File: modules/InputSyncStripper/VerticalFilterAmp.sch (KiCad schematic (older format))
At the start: 12 parts

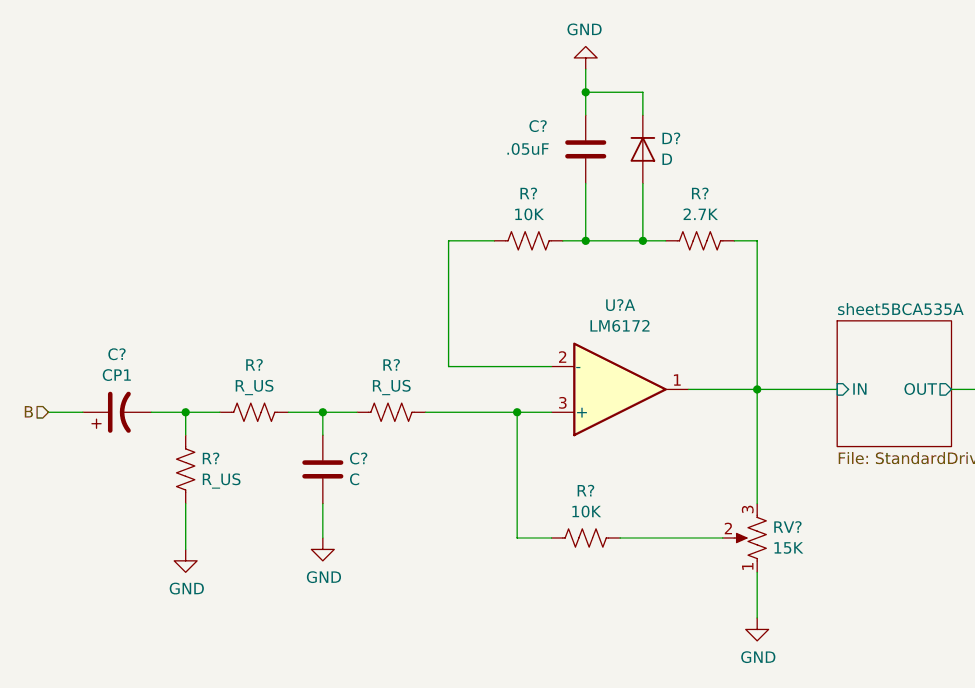
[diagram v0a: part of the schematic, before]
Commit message: fix some ERC issues; assign symbols
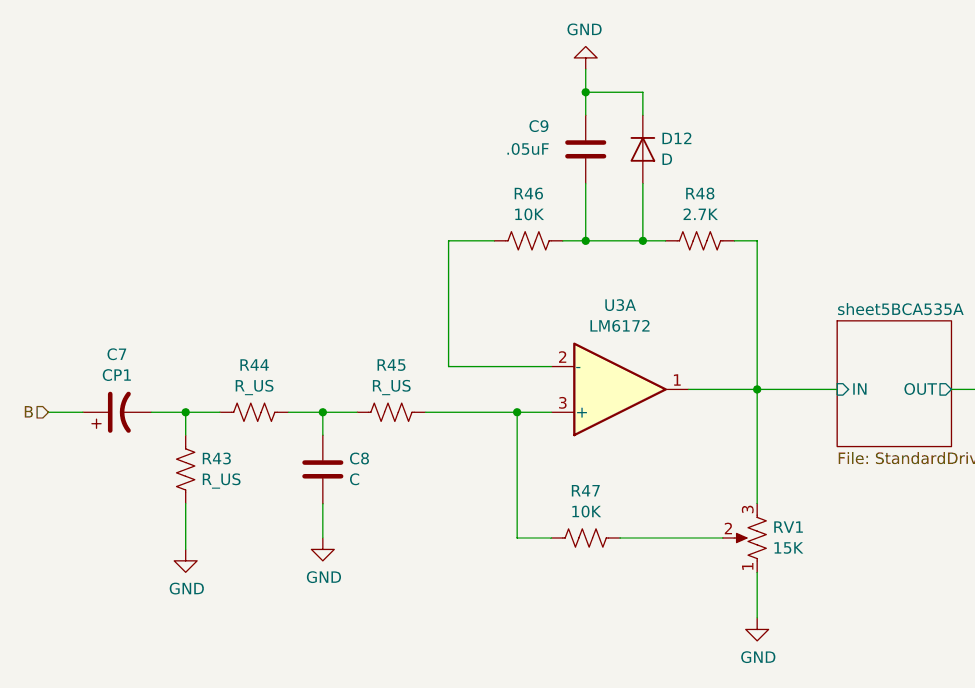
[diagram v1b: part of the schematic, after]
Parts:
- gave numbers to parts that had none: 12
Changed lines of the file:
@@
 EESchema Schematic File Version 4
-LIBS:SIP-cache
+LIBS:InputSyncStripper-cache
 EELAYER 26 0
 EELAYER END
@@
 $EndDescr
 $Comp
-L Amplifier_Operational:LM6172 U?
+L Amplifier_Operational:LM6172 U3
 U 1 1 5BCA52BB
 P 4700 3700
-F 0 "U?" H 4700 3333 50  0000 C CNN
+F 0 "U3" H 4700 3333 50  0000 C CNN
 F 1 "LM6172" H 4700 3424 50  0000 C CNN
 F 2 "" H 4700 3700 50  0001 C CNN
@@
 $EndSheet
 $Comp
-L Device:R_US R?
+L Device:R_US R48
 U 1 1 5BCA537D
 P 5050 3050
-F 0 "R?" V 4845 3050 50  0000 C CNN
+F 0 "R48" V 4845 3050 50  0000 C CNN
 F 1 "2.7K" V 4936 3050 50  0000 C CNN
 F 2 "" V 5090 3040 50  0001 C CNN
@@
 $EndComp
 $Comp
-L Device:R_US R?
+L Device:R_US R46
 U 1 1 5BCA543E
 P 4300 3050
-F 0 "R?" V 4095 3050 50  0000 C CNN
+F 0 "R46" V 4095 3050 50  0000 C CNN
 F 1 "10K" V 4186 3050 50  0000 C CNN
 F 2 "" V 4340 3040 50  0001 C CNN
@@
 Connection ~ 5300 3700
 $Comp
-L Device:R_POT_US RV?
+L Device:R_POT_US RV1
 U 1 1 5BCA5542
 P 5300 4350
-F 0 "RV?" H 5232 4304 50  0000 R CNN
+F 0 "RV1" H 5232 4304 50  0000 R CNN
 F 1 "15K" H 5232 4395 50  0000 R CNN
 F 2 "" H 5300 4350 50  0001 C CNN
@@
 $EndComp
 $Comp
-L power:GND #PWR?
+L power:GND #PWR023
 U 1 1 5BCA55A7
 P 5300 4700
-F 0 "#PWR?" H 5300 4450 50  0001 C CNN
+F 0 "#PWR023" H 5300 4450 50  0001 C CNN
 F 1 "GND" H 5305 4527 50  0000 C CNN
 F 2 "" H 5300 4700 50  0001 C CNN
@@
 	5300 4200 5300 3700
 $Comp
-L Device:R_US R?
+L Device:R_US R47
 U 1 1 5BCA5671
 P 4550 4350
-F 0 "R?" V 4345 4350 50  0000 C CNN
+F 0 "R47" V 4345 4350 50  0000 C CNN
 F 1 "10K" V 4436 4350 50  0000 C CNN
 F 2 "" V 4590 4340 50  0001 C CNN
@@
 	4250 3800 4400 3800
 $Comp
-L Device:C C?
+L Device:C C9
 U 1 1 5BCA585A
 P 4550 2650
-F 0 "C?" H 4300 2750 50  0000 L CNN
+F 0 "C9" H 4300 2750 50  0000 L CNN
 F 1 ".05uF" H 4200 2650 50  0000 L CNN
 F 2 "" H 4588 2500 50  0001 C CNN
@@
 $EndComp
 $Comp
-L Device:D D?
+L Device:D D12
 U 1 1 5BCA5A8B
 P 4800 2650
-F 0 "D?" V 4754 2729 50  0000 L CNN
+F 0 "D12" V 4754 2729 50  0000 L CNN
 F 1 "D" V 4845 2729 50  0000 L CNN
 F 2 "" H 4800 2650 50  0001 C CNN
@@
 $EndComp
 $Comp
-L power:GND #PWR?
+L power:GND #PWR022
 U 1 1 5BCA5BA5
 P 4550 2300
-F 0 "#PWR?" H 4550 2050 50  0001 C CNN
+F 0 "#PWR022" H 4550 2050 50  0001 C CNN
 F 1 "GND" H 4555 2127 50  0000 C CNN
 F 2 "" H 4550 2300 50  0001 C CNN
@@
 	4800 3050 4900 3050
 $Comp
-L Device:R_US R?
+L Device:R_US R45
 U 1 1 5BCA6118
 P 3700 3800
-F 0 "R?" V 3495 3800 50  0000 C CNN
+F 0 "R45" V 3495 3800 50  0000 C CNN
 F 1 "R_US" V 3586 3800 50  0000 C CNN
 F 2 "" V 3740 3790 50  0001 C CNN
@@
 $EndComp
 $Comp
-L Device:R_US R?
+L Device:R_US R44
 U 1 1 5BCA6199
 P 3100 3800
-F 0 "R?" V 2895 3800 50  0000 C CNN
+F 0 "R44" V 2895 3800 50  0000 C CNN
 F 1 "R_US" V 2986 3800 50  0000 C CNN
 F 2 "" V 3140 3790 50  0001 C CNN
@@
 $EndComp
 $Comp
-L Device:R_US R?
+L Device:R_US R43
 U 1 1 5BCA61F8
 P 2800 4050
-F 0 "R?" H 2868 4096 50  0000 L CNN
+F 0 "R43" H 2868 4096 50  0000 L CNN
 F 1 "R_US" H 2868 4005 50  0000 L CNN
 F 2 "" V 2840 4040 50  0001 C CNN
@@
 $EndComp
 $Comp
-L Device:CP1 C?
+L Device:CP1 C7
 U 1 1 5BCA625D
 P 2500 3800
-F 0 "C?" V 2752 3800 50  0000 C CNN
+F 0 "C7" V 2752 3800 50  0000 C CNN
 F 1 "CP1" V 2661 3800 50  0000 C CNN
 F 2 "" H 2500 3800 50  0001 C CNN
@@
 $EndComp
 $Comp
-L Device:C C?
+L Device:C C8
 U 1 1 5BCA6305
 P 3400 4050
-F 0 "C?" H 3515 4096 50  0000 L CNN
+F 0 "C8" H 3515 4096 50  0000 L CNN
 F 1 "C" H 3515 4005 50  0000 L CNN
 F 2 "" H 3438 3900 50  0001 C CNN
@@
 $EndComp
 $Comp
-L power:GND #PWR?
+L power:GND #PWR020
 U 1 1 5BCA63C4
 P 2800 4400
-F 0 "#PWR?" H 2800 4150 50  0001 C CNN
+F 0 "#PWR020" H 2800 4150 50  0001 C CNN
 F 1 "GND" H 2805 4227 50  0000 C CNN
 F 2 "" H 2800 4400 50  0001 C CNN
@@
 $EndComp
 $Comp
-L power:GND #PWR?
+L power:GND #PWR021
 U 1 1 5BCA640A
 P 3400 4350
-F 0 "#PWR?" H 3400 4100 50  0001 C CNN
+F 0 "#PWR021" H 3400 4100 50  0001 C CNN
 F 1 "GND" H 3405 4177 50  0000 C CNN
 F 2 "" H 3400 4350 50  0001 C CNN

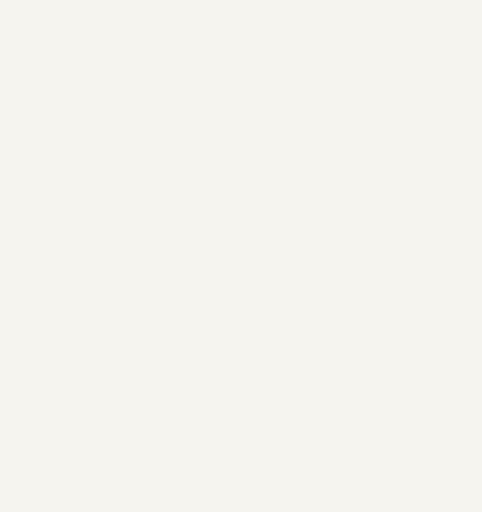
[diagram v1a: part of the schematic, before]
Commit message: added power pins for opamps and tied inputs of unused amp
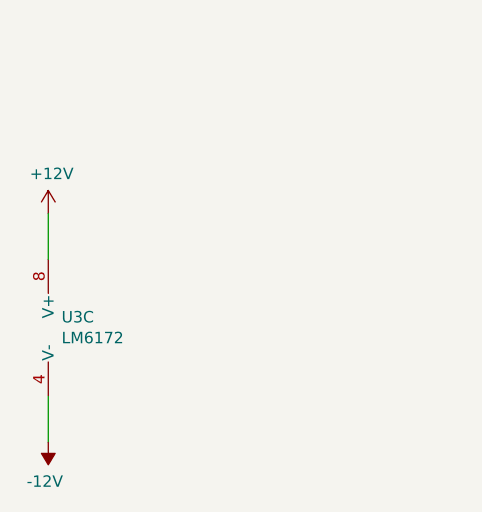
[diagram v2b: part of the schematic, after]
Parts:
- added unit 3 of U3
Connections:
- new net +12V: U3.8 (V+)
- new net -12V: U3.4 (V-)
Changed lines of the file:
@@
 Wire Wire Line
 	6150 3700 6500 3700
+$Comp
+L Amplifier_Operational:LM6172 U?
+U 3 1 5BCFED9F
+P 1150 7000
+AR Path="/5BC7EA60/5BCFED9F" Ref="U?"  Part="3"
+AR Path="/5BCA510D/5BCFED9F" Ref="U3"  Part="3"
+F 0 "U3" H 1108 7046 50  0000 L CNN
+F 1 "LM6172" H 1108 6955 50  0000 L CNN
+F 2 "" H 1150 7000 50  0001 C CNN
+F 3 "http://www.ti.com/lit/ds/symlink/lm6172.pdf" H 1150 7000 50  0001 C CNN
+	3    1150 7000
+	1    0    0    -1
+$EndComp
+$Comp
+L power:+12V #PWR?
+U 1 1 5BCFEDA6
+P 1050 6500
+AR Path="/5BC7EA60/5BCFEDA6" Ref="#PWR?"  Part="1"
+AR Path="/5BCA510D/5BCFEDA6" Ref="#PWR0114"  Part="1"
+F 0 "#PWR0114" H 1050 6350 50  0001 C CNN
+F 1 "+12V" H 1065 6673 50  0000 C CNN
+F 2 "" H 1050 6500 50  0001 C CNN
+F 3 "" H 1050 6500 50  0001 C CNN
+	1    1050 6500
+	1    0    0    -1
+$EndComp
+$Comp
+L power:-12V #PWR?
+U 1 1 5BCFEDAC
+P 1050 7500
+AR Path="/5BC7EA60/5BCFEDAC" Ref="#PWR?"  Part="1"
+AR Path="/5BCA510D/5BCFEDAC" Ref="#PWR0115"  Part="1"
+F 0 "#PWR0115" H 1050 7600 50  0001 C CNN
+F 1 "-12V" H 1065 7673 50  0000 C CNN
+F 2 "" H 1050 7500 50  0001 C CNN
+F 3 "" H 1050 7500 50  0001 C CNN
+	1    1050 7500
+	-1   0    0    1
+$EndComp
+Wire Wire Line
+	1050 7500 1050 7300
+Wire Wire Line
+	1050 6700 1050 6500
 $EndSCHEMATC

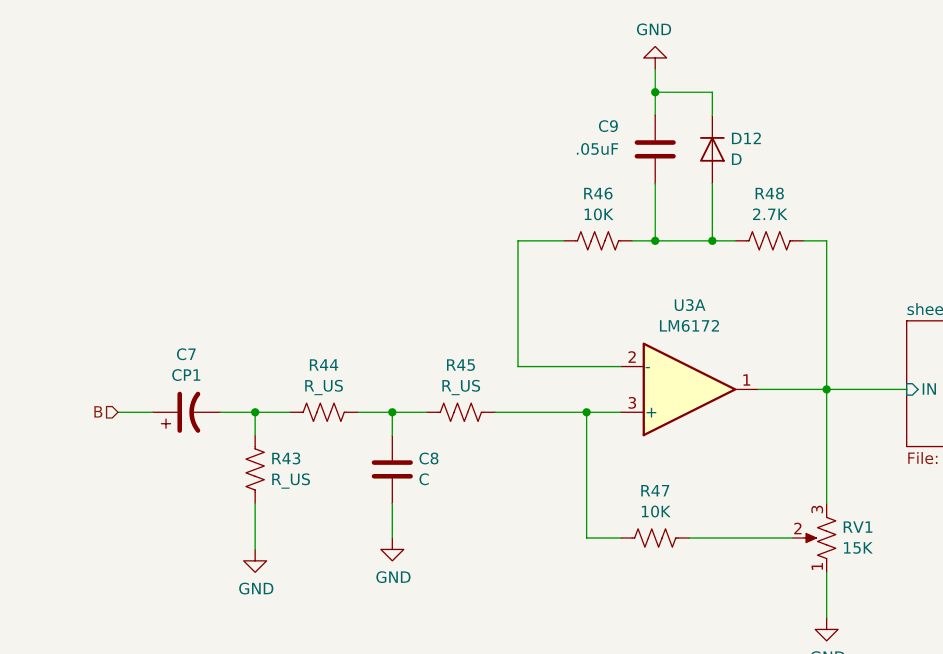
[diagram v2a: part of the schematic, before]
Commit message: Find and fix missing values
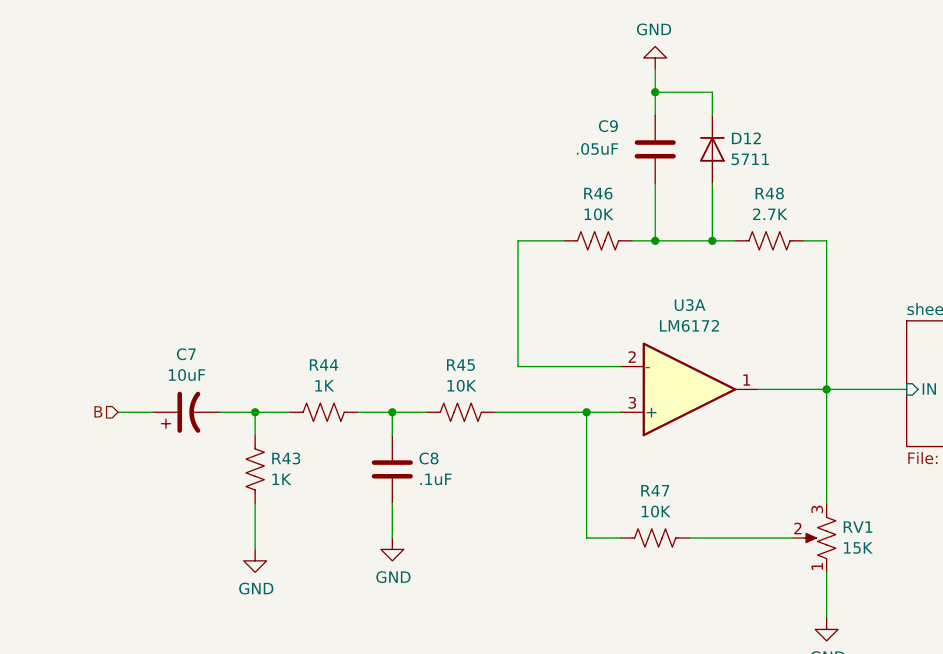
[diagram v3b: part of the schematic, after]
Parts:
- C7: value CP1 -> 10uF
- C8: value C -> .1uF
- D12: value D -> 5711
- R43, R44: value R_US -> 1K
- R45: value R_US -> 10K
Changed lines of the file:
@@
 P 4800 2650
 F 0 "D12" V 4754 2729 50  0000 L CNN
-F 1 "D" V 4845 2729 50  0000 L CNN
+F 1 "5711" V 4845 2729 50  0000 L CNN
 F 2 "" H 4800 2650 50  0001 C CNN
 F 3 "~" H 4800 2650 50  0001 C CNN
@@
 P 3700 3800
 F 0 "R45" V 3495 3800 50  0000 C CNN
-F 1 "R_US" V 3586 3800 50  0000 C CNN
+F 1 "10K" V 3586 3800 50  0000 C CNN
 F 2 "" V 3740 3790 50  0001 C CNN
 F 3 "~" H 3700 3800 50  0001 C CNN
@@
 P 3100 3800
 F 0 "R44" V 2895 3800 50  0000 C CNN
-F 1 "R_US" V 2986 3800 50  0000 C CNN
+F 1 "1K" V 2986 3800 50  0000 C CNN
 F 2 "" V 3140 3790 50  0001 C CNN
 F 3 "~" H 3100 3800 50  0001 C CNN
@@
 P 2800 4050
 F 0 "R43" H 2868 4096 50  0000 L CNN
-F 1 "R_US" H 2868 4005 50  0000 L CNN
+F 1 "1K" H 2868 4005 50  0000 L CNN
 F 2 "" V 2840 4040 50  0001 C CNN
 F 3 "~" H 2800 4050 50  0001 C CNN
@@
 P 2500 3800
 F 0 "C7" V 2752 3800 50  0000 C CNN
-F 1 "CP1" V 2661 3800 50  0000 C CNN
+F 1 "10uF" V 2661 3800 50  0000 C CNN
 F 2 "" H 2500 3800 50  0001 C CNN
 F 3 "~" H 2500 3800 50  0001 C CNN
@@
 P 3400 4050
 F 0 "C8" H 3515 4096 50  0000 L CNN
-F 1 "C" H 3515 4005 50  0000 L CNN
+F 1 ".1uF" H 3515 4005 50  0000 L CNN
 F 2 "" H 3438 3900 50  0001 C CNN
 F 3 "~" H 3400 4050 50  0001 C CNN

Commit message: building out footprints/BOM
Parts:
- C7: footprint (none) -> Capacitor_SMD:CP_Elec_5x5.4
- C8, C9: footprint (none) -> Capacitor_SMD:C_0805_2012Metric_Pad1.15x1.40mm_HandSolder
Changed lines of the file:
@@
 F 0 "C9" H 4300 2750 50  0000 L CNN
 F 1 ".05uF" H 4200 2650 50  0000 L CNN
-F 2 "" H 4588 2500 50  0001 C CNN
+F 2 "Capacitor_SMD:C_0805_2012Metric_Pad1.15x1.40mm_HandSolder" H 4588 2500 50  0001 C CNN
 F 3 "~" H 4550 2650 50  0001 C CNN
 	1    4550 2650
@@
 F 0 "C7" V 2752 3800 50  0000 C CNN
 F 1 "10uF" V 2661 3800 50  0000 C CNN
-F 2 "" H 2500 3800 50  0001 C CNN
-F 3 "~" H 2500 3800 50  0001 C CNN
+F 2 "Capacitor_SMD:CP_Elec_5x5.4" H 2500 3800 50  0001 C CNN
+F 3 "https://industrial.panasonic.com/cdbs/www-data/pdf/RDE0000/ABA0000C1145.pdf" H 2500 3800 50  0001 C CNN
 	1    2500 3800
 	0    -1   -1   0
@@
 F 0 "C8" H 3515 4096 50  0000 L CNN
 F 1 ".1uF" H 3515 4005 50  0000 L CNN
-F 2 "" H 3438 3900 50  0001 C CNN
+F 2 "Capacitor_SMD:C_0805_2012Metric_Pad1.15x1.40mm_HandSolder" H 3438 3900 50  0001 C CNN
 F 3 "~" H 3400 4050 50  0001 C CNN
 	1    3400 4050
